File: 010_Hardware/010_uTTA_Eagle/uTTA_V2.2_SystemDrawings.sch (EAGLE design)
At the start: 3 parts

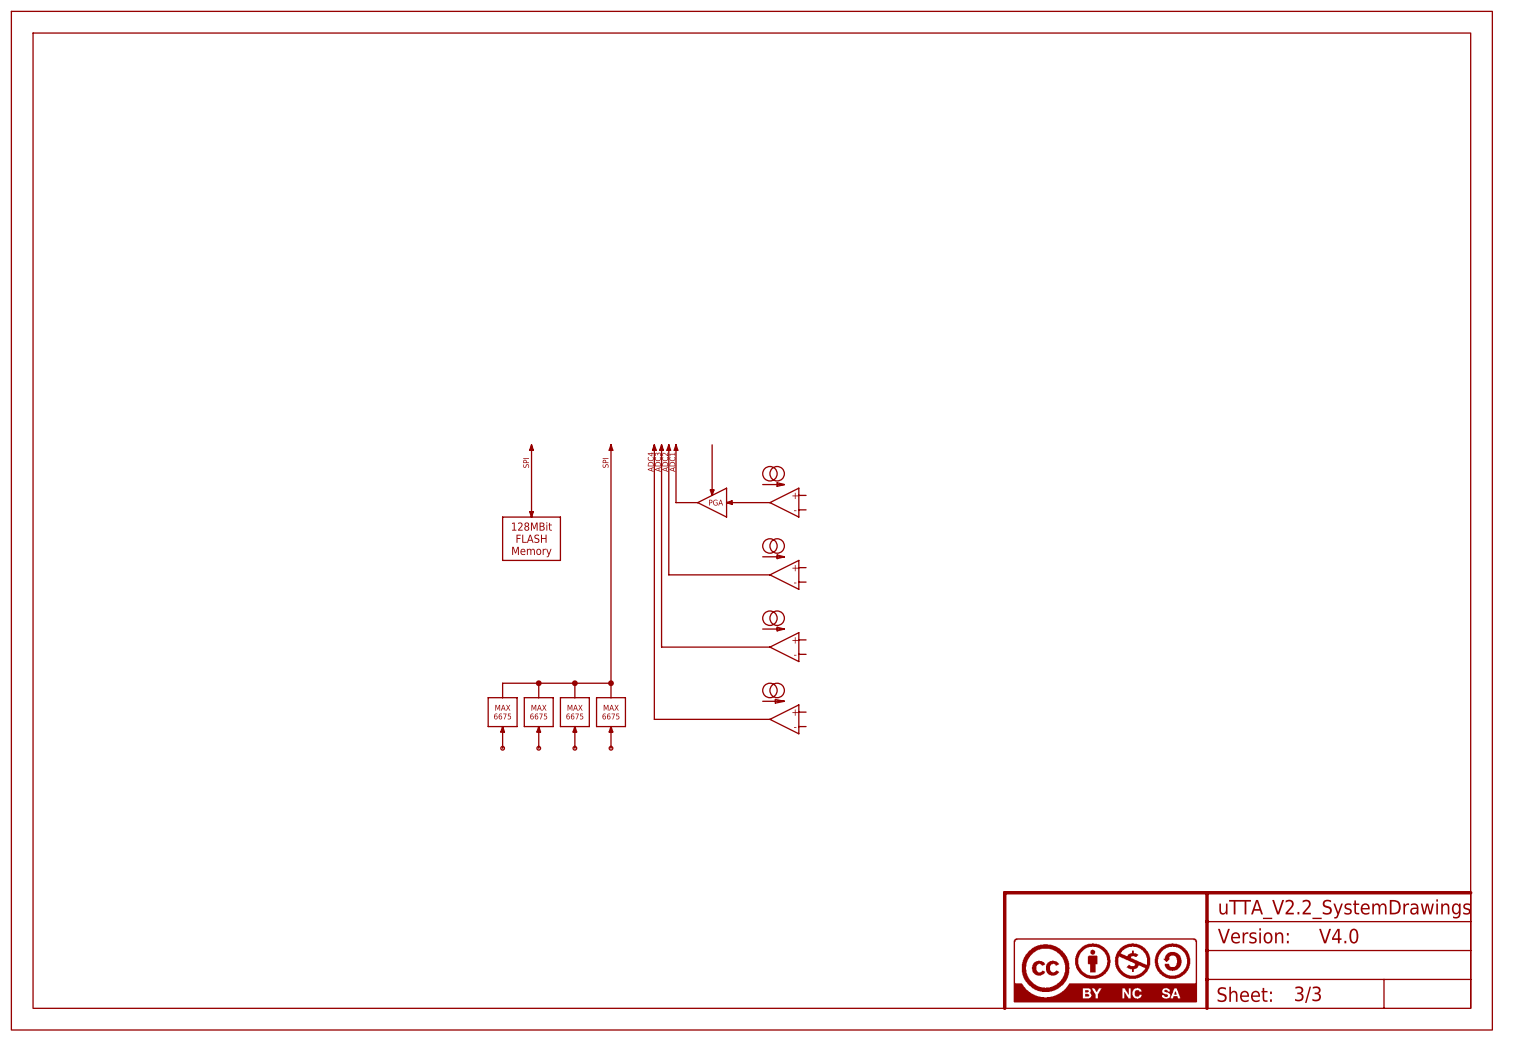
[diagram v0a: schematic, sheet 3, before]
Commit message: Update to uTTA Version 2.2
Full update of both PCBs to HW Version 2.2:
Removed spare FLASH Memory
Adjusted Position of LEDs and Buttons
Cleanup of layout
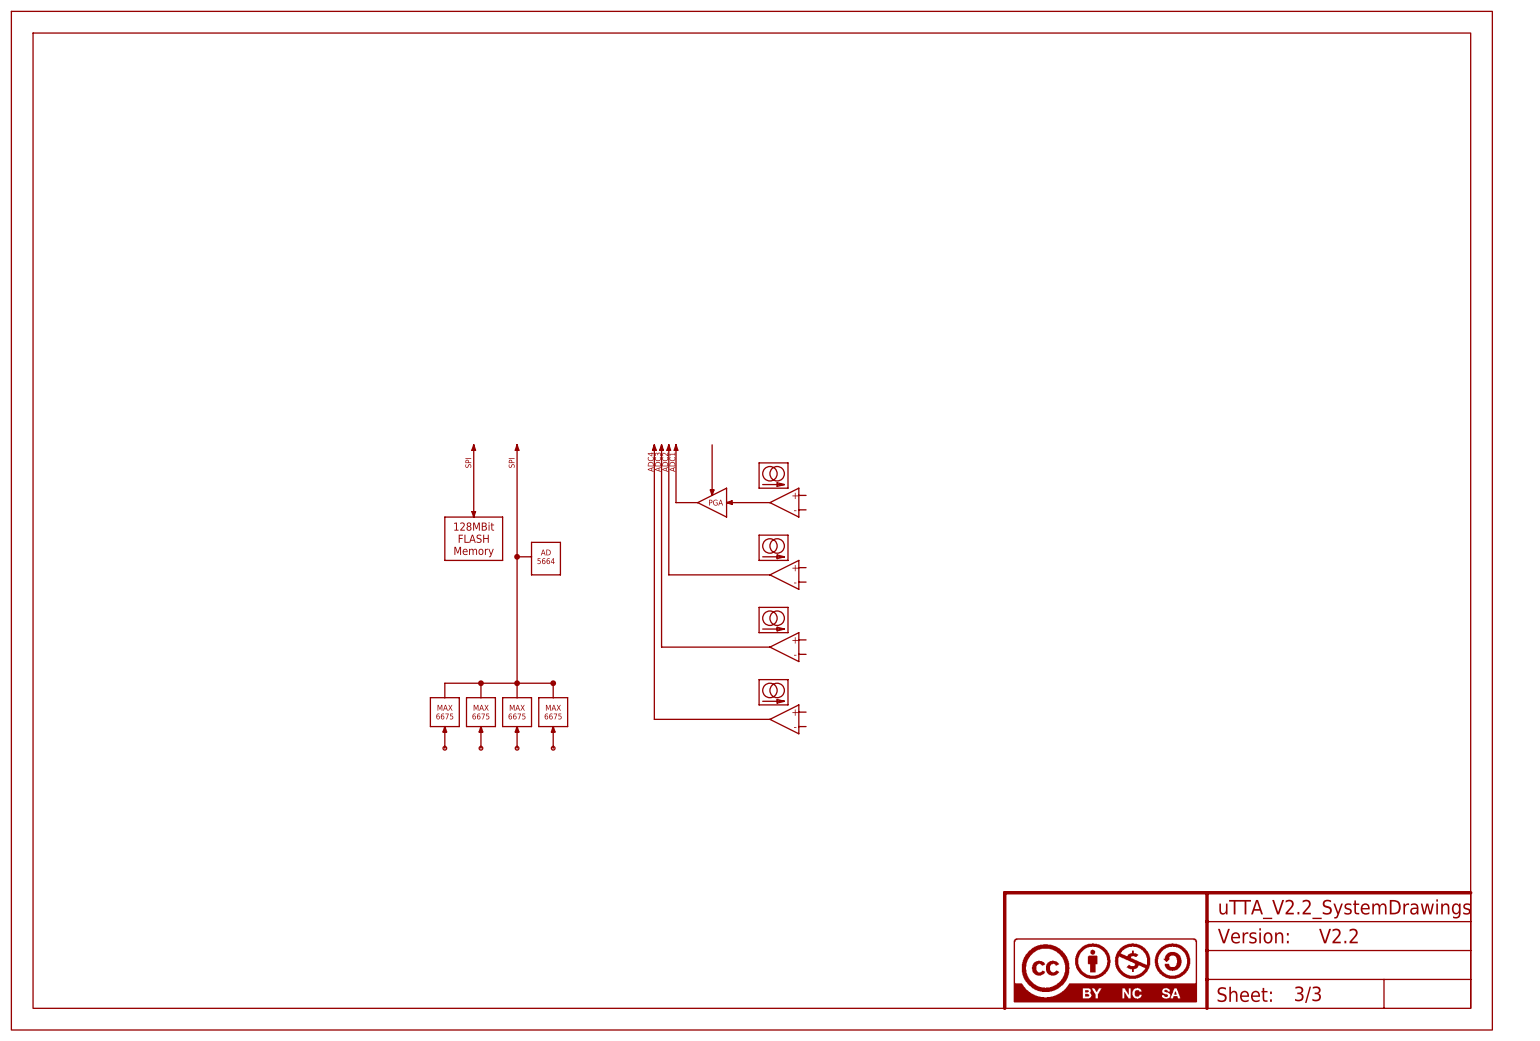
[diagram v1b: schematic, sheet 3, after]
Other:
- note added: "AD 5664"
- note added: "Imax = 15A"
- note added: "uTTA_V2.2 Measure"
- note added: "uTTA_V2.2 Power"
- note removed: "Imax = 30A"
- note removed: "uTTA_V4 Power"
